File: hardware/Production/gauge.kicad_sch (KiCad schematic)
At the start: 68 parts, among them J102 Cell 1 NTC wires, J105 Cell 2 NTC wires, J106 Cell 3 NTC wires, J107 Cell 4 NTC wires, J108 PACK- power wire, J109 CELL1 sense wire, J110 CELL2 sense wire, J111 CELL3 sense wire, J112 PACK+ power wire, J113 LOAD PACK_P, J114 LOAD GND, J115 1N Kelvin wire, J116 4P Kelvin wire, Q101 BSC007N04LS6, Q102 BSC007N04LS6, Q103 AO3400A, Q104 AO3400A, U101 BQ40Z50RSMR-R2, U102 BQ294700DSGR

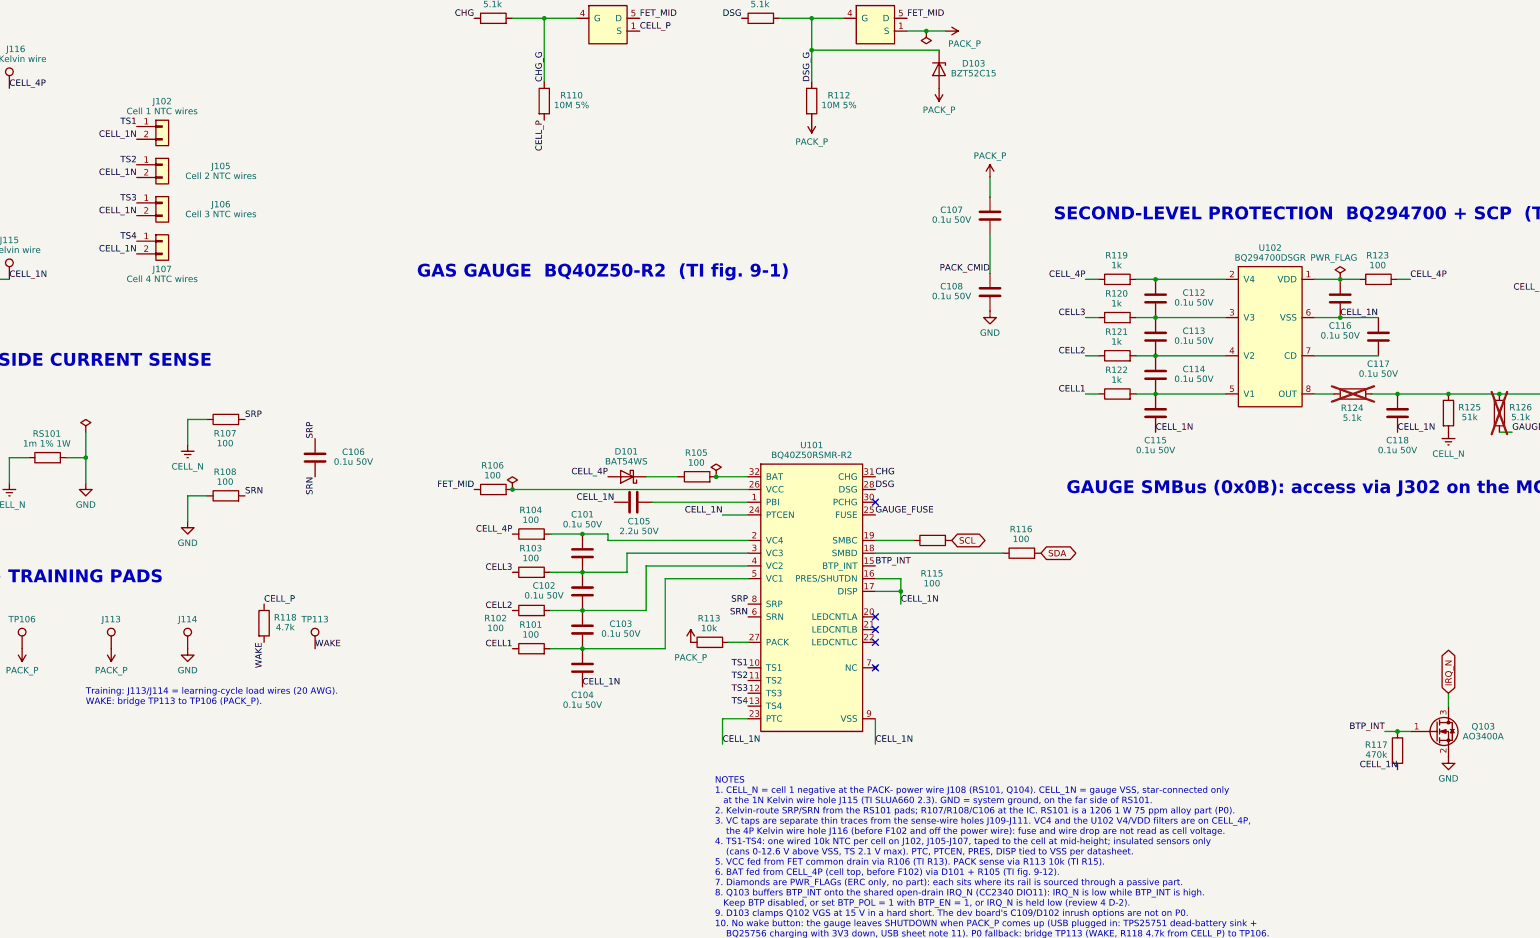
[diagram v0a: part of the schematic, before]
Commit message: Front-cell NTCs: SMD on the board (TH101 / TH104) instead of wired beads
TS1 / TS4 move from wired beads on the cans (J102 / J107) to 0402 NTCs
(NCP15XH103F03RC) on B.Cu in the outer bottom corner of each gap-filler
zone, |y| 15.5 mm, z 29 mm, outboard of port 1's BQ25756. In the 3-D model
with the 10-27 stage layout they read 0.6-3.8 K above the hottest can point
and never below it. The discharge ramp moves up 2 K (44 -> 48 C) to keep
the same energy; charge ramp and gauge limits unchanged.

- gauge.kicad_sch: J102 / J107 -> TH101 / TH104, sheet note 4
- Monolith.kicad_pcb: TH101 / TH104 placed and locked on B.Cu, J102 / J107
  and KO_B_ntc_* removed, KO_B_gap_filler_L/_R notched for the parts
- monolith_shell sb_ntc_smd(), make_board / make_production follow it
- spec, firmware policy, assembly, bring-up, board README, step 2 render
- smd.py: p0b layout, spot probes and policy runs; smd-ntc.md rewritten

Co-Authored-By: Claude Opus 5.5 <noreply@anthropic.com>
Claude-Session: https://claude.ai/code/session_01LzE9uxopd3CrLAEeFamvpR
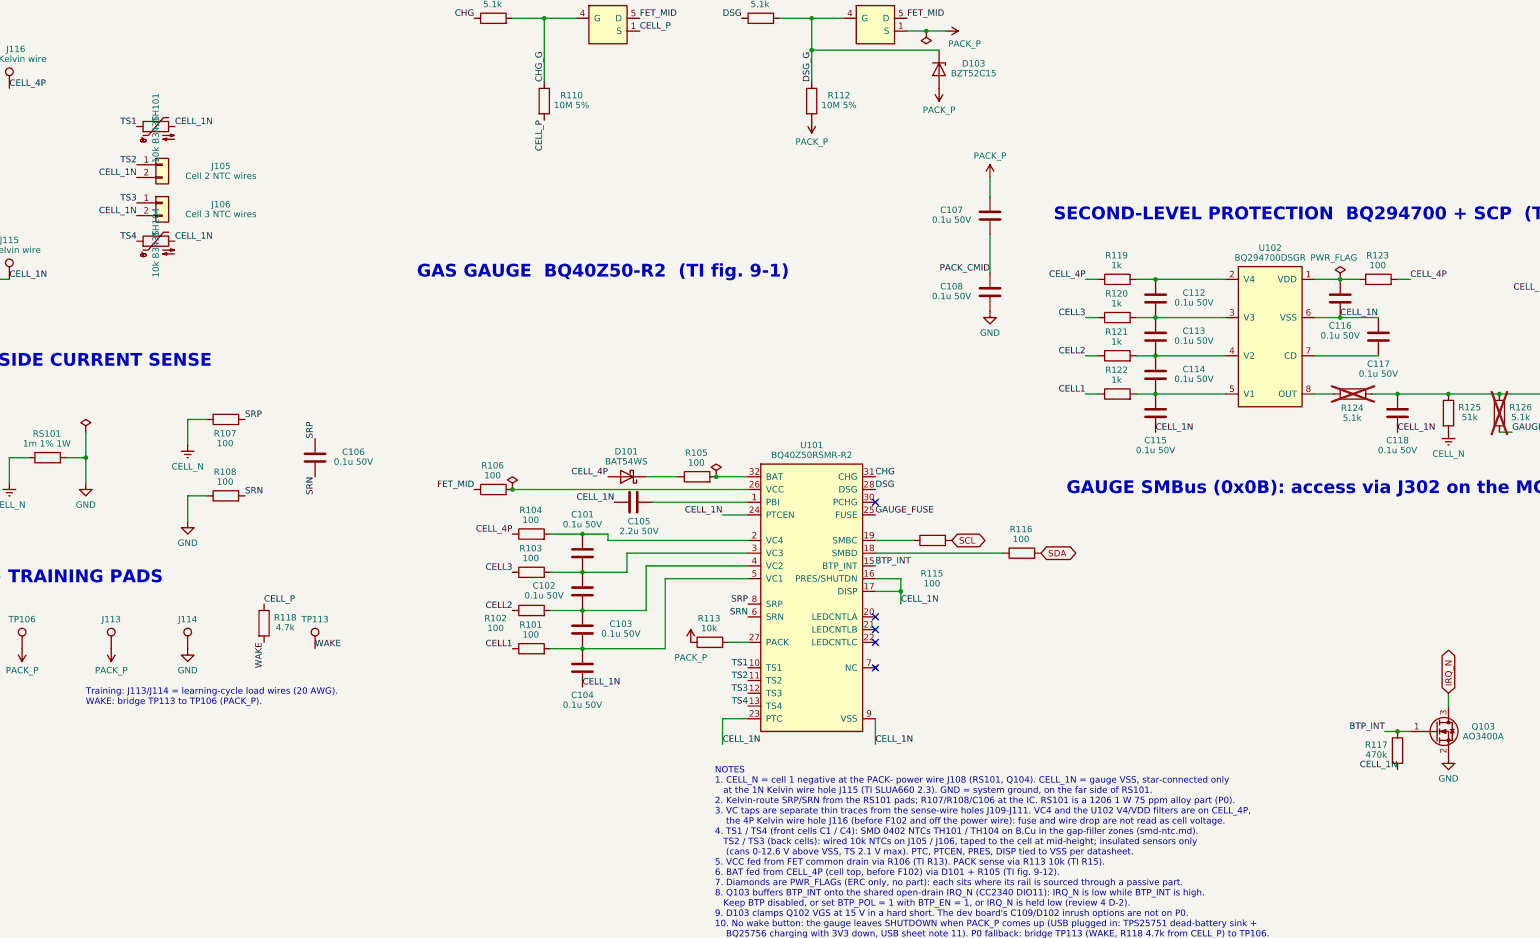
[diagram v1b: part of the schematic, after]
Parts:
- TH101: renamed from J102; value Cell 1 NTC wires -> 10k B3435; footprint Connector_Wire:SolderWire-0.15sqmm_1x02_P4mm_D0.5mm_OD1.5mm -> Resistor_SMD:R_0402_1005Metric; symbol Connector_Generic:Conn_01x02 -> Device:Thermistor_NTC; LCSC (none) -> C77131; MPN PZ254V-11-02P -> NCP15XH103F03RC; Notes Wired 10k B3435 NTC (Semitec 103AT-2 class, epoxy bead with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 -> Front-cell NTC, SMD on B.Cu in the outer bottom corner of t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; Sourcing Hand-solder, not JLC assembled (through-hole; LCSC C492401 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 -> (none)
- TH104: renamed from J107; value Cell 4 NTC wires -> 10k B3435; footprint Connector_Wire:SolderWire-0.15sqmm_1x02_P4mm_D0.5mm_OD1.5mm -> Resistor_SMD:R_0402_1005Metric; symbol Connector_Generic:Conn_01x02 -> Device:Thermistor_NTC; LCSC (none) -> C77131; MPN PZ254V-11-02P -> NCP15XH103F03RC; Notes Wired 10k B3435 NTC (Semitec 103AT-2 class, epoxy bead with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 -> Front-cell NTC, SMD on B.Cu in the outer bottom corner of t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; Sourcing Hand-solder, not JLC assembled (through-hole; LCSC C492401 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 -> (none)
